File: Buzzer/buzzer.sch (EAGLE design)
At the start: 1 part

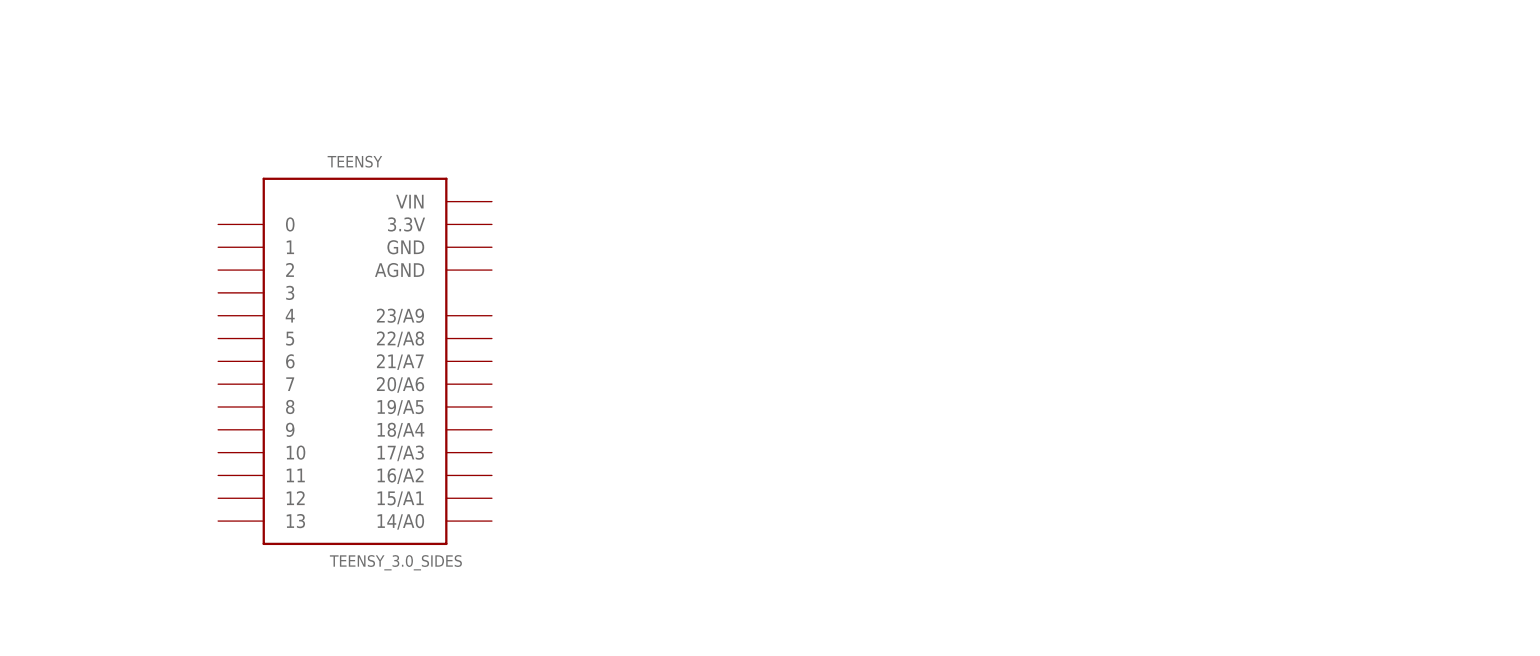
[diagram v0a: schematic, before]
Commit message: Done Eagle schematic, still needs board
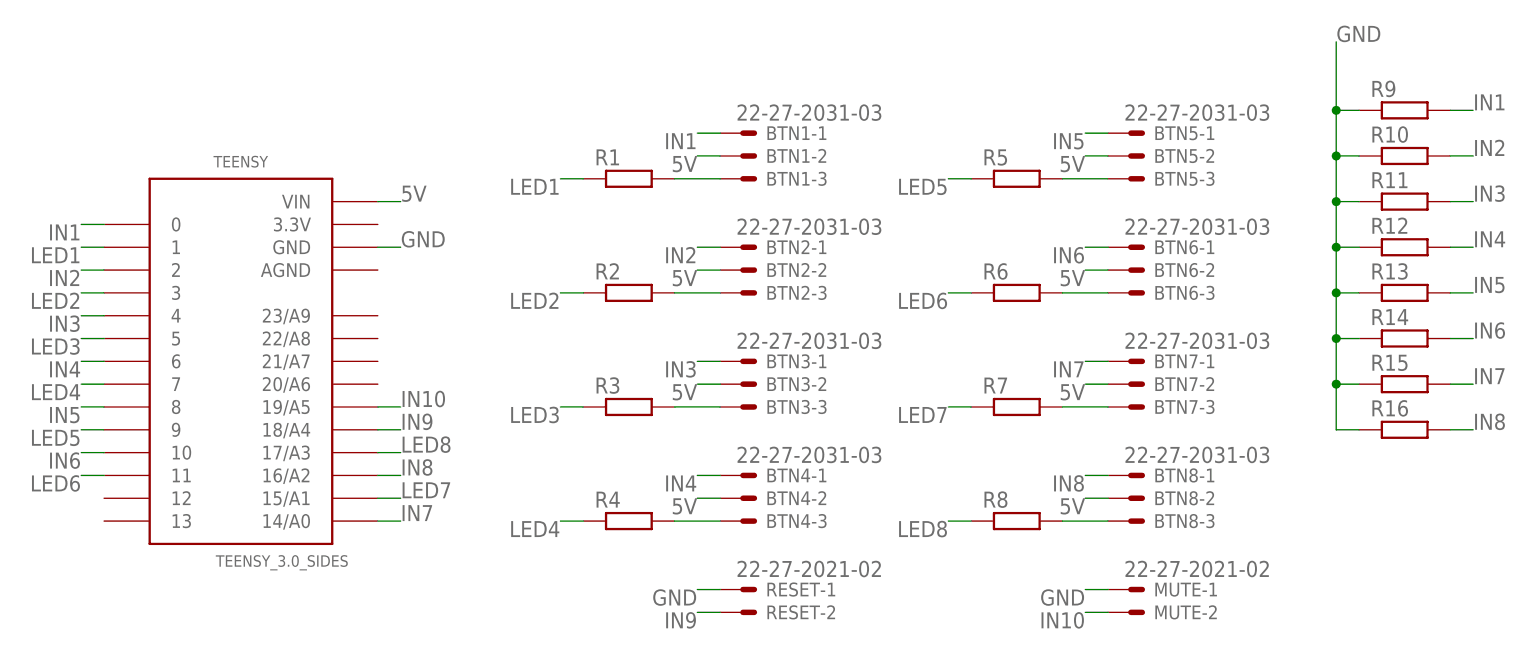
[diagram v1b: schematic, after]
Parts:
- added BTN1, BTN2, BTN3, BTN4, BTN5, BTN6, BTN7, BTN8: 22-27-2031-03, con-molex:22-27-2031-03
- added MUTE, RESET: 22-27-2021-02, con-molex:22-27-2021-02
- added R1, R10, R11, R12, R13, R14, R15, R16, R2, R3, R4, R5, R6, R7, R8, R9: (no value), eagle-ltspice:R0207/10
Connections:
- new net 5V: BTN1-2.S, BTN2-2.S, BTN3-2.S, BTN4-2.S, BTN5-2.S, BTN6-2.S, BTN7-2.S, BTN8-2.S, TEENSY.VIN
- new net GND: MUTE-1.S, R10.1, R11.1, R12.1, R13.1, R14.1, R15.1, R16.1, R9.1, RESET-1.S, TEENSY.GND
- new net IN1: BTN1-1.S, R9.2, TEENSY.0
- new net IN10: MUTE-2.S, TEENSY.19/A5
- new net IN2: BTN2-1.S, R10.2, TEENSY.2
- new net IN3: BTN3-1.S, R11.2, TEENSY.4
- new net IN4: BTN4-1.S, R12.2, TEENSY.6
- new net IN5: BTN5-1.S, R13.2, TEENSY.8
- new net IN6: BTN6-1.S, R14.2, TEENSY.10
- new net IN7: BTN7-1.S, R15.2, TEENSY.14/A0
- new net IN8: BTN8-1.S, R16.2, TEENSY.16/A2
- new net IN9: RESET-2.S, TEENSY.18/A4
- new net LED1: R1.1, TEENSY.1
- new net LED2: R2.1, TEENSY.3
- new net LED3: R3.1, TEENSY.5
- new net LED4: R4.1, TEENSY.7
- new net LED5: R5.1, TEENSY.9
- new net LED6: R6.1, TEENSY.11
- new net LED7: R7.1, TEENSY.15/A1
- new net LED8: R8.1, TEENSY.17/A3
- new net N$1: BTN1-3.S, R1.2
- new net N$18: BTN6-3.S, R6.2
- new net N$2: BTN4-3.S, R4.2
- new net N$3: BTN5-3.S, R5.2
- new net N$4: BTN7-3.S, R7.2
- new net N$5: BTN8-3.S, R8.2
- new net N$6: BTN2-3.S, R2.2
- new net N$9: BTN3-3.S, R3.2
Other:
- moved on the sheet: TEENSY
